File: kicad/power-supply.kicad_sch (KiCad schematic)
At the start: 6 parts, among them U8 M3406

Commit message: added title to all circuit diagrams and sub-circuit diagrams, and PDF export
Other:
- title: (none) -> step-down voltage regulator
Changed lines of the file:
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@@
 (kicad_sch (version 20211123) (generator eeschema)
   (paper "A4")
+  (title_block
+    (title "step-down voltage regulator")
+  )
   (junction (at 133.35 72.39) (diameter 0) (color 0 0 0 0)
   )

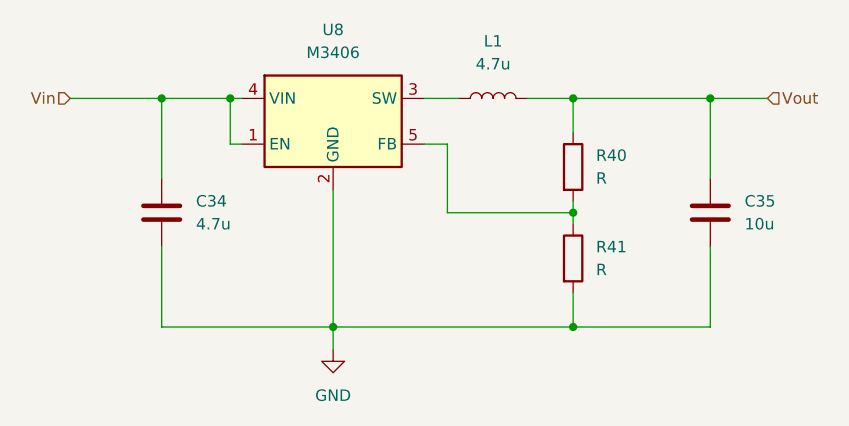
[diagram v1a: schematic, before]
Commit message: new flash, and IEC interface added
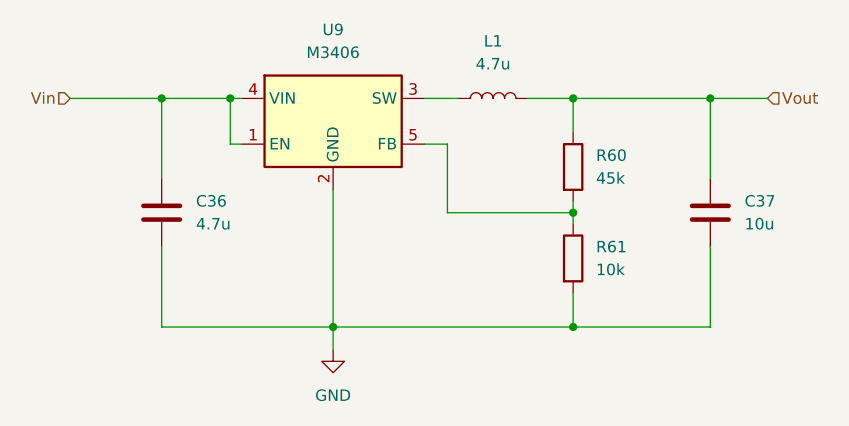
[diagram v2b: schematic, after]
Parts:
- R60: renamed from R40; value R -> 45k; footprint Resistor_SMD:R_0402_1005Metric -> Resistor_SMD:R_0805_2012Metric
- R61: renamed from R41; value R -> 10k; footprint Resistor_SMD:R_0402_1005Metric -> Resistor_SMD:R_0805_2012Metric
- renumbered C34 to C36, C35 to C37, U8 to U9
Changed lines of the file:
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@@
   (symbol (lib_id "Device:R") (at 133.35 67.31 0) (unit 1)
     (in_bom yes) (on_board yes) (fields_autoplaced)
-    (property "Reference" "R40" (id 0) (at 135.89 66.0399 0)
+    (property "Reference" "R60" (id 0) (at 135.89 66.0399 0)
       (effects (font (size 1.27 1.27)) (justify left))
     )
-    (property "Value" "R" (id 1) (at 135.89 68.5799 0)
+    (property "Value" "45k" (id 1) (at 135.89 68.5799 0)
       (effects (font (size 1.27 1.27)) (justify left))
     )
-    (property "Footprint" "Resistor_SMD:R_0402_1005Metric" (id 2) (at 131.572 67.31 90)
+    (property "Footprint" "Resistor_SMD:R_0805_2012Metric" (id 2) (at 131.572 67.31 90)
       (effects (font (size 1.27 1.27)) hide)
     )
@@
   (symbol (lib_id "Device:C") (at 87.63 72.39 0) (unit 1)
     (in_bom yes) (on_board yes) (fields_autoplaced)
-    (property "Reference" "C34" (id 0) (at 91.44 71.1199 0)
+    (property "Reference" "C36" (id 0) (at 91.44 71.1199 0)
       (effects (font (size 1.27 1.27)) (justify left))
     )
@@
   (symbol (lib_id "power:GND") (at 106.68 87.63 0) (unit 1)
     (in_bom yes) (on_board yes) (fields_autoplaced)
-    (property "Reference" "#PWR076" (id 0) (at 106.68 93.98 0)
+    (property "Reference" "#PWR082" (id 0) (at 106.68 93.98 0)
       (effects (font (size 1.27 1.27)) hide)
     )
@@
   (symbol (lib_id "Device:C") (at 148.59 72.39 0) (unit 1)
     (in_bom yes) (on_board yes) (fields_autoplaced)
-    (property "Reference" "C35" (id 0) (at 152.4 71.1199 0)
+    (property "Reference" "C37" (id 0) (at 152.4 71.1199 0)
       (effects (font (size 1.27 1.27)) (justify left))
     )
@@
   (symbol (lib_id "Regulator_Switching:PAM2301CAABADJ") (at 106.68 62.23 0) (unit 1)
     (in_bom yes) (on_board yes) (fields_autoplaced)
-    (property "Reference" "U8" (id 0) (at 106.68 52.07 0))
+    (property "Reference" "U9" (id 0) (at 106.68 52.07 0))
     (property "Value" "M3406" (id 1) (at 106.68 54.61 0))
     (property "Footprint" "Package_TO_SOT_SMD:TSOT-23-5" (id 2) (at 107.95 68.58 0)
@@
   (symbol (lib_id "Device:R") (at 133.35 77.47 0) (unit 1)
     (in_bom yes) (on_board yes) (fields_autoplaced)
-    (property "Reference" "R41" (id 0) (at 135.89 76.1999 0)
+    (property "Reference" "R61" (id 0) (at 135.89 76.1999 0)
       (effects (font (size 1.27 1.27)) (justify left))
     )
-    (property "Value" "R" (id 1) (at 135.89 78.7399 0)
+    (property "Value" "10k" (id 1) (at 135.89 78.7399 0)
       (effects (font (size 1.27 1.27)) (justify left))
     )
-    (property "Footprint" "Resistor_SMD:R_0402_1005Metric" (id 2) (at 131.572 77.47 90)
+    (property "Footprint" "Resistor_SMD:R_0805_2012Metric" (id 2) (at 131.572 77.47 90)
       (effects (font (size 1.27 1.27)) hide)
     )

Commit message: circuit improvements fixed the level shifter circuit, added the shield pins to the reset button, and replaced the IEC circuit with unused pins of the 16 bit level shifter, and a new 6 channel open collector driver
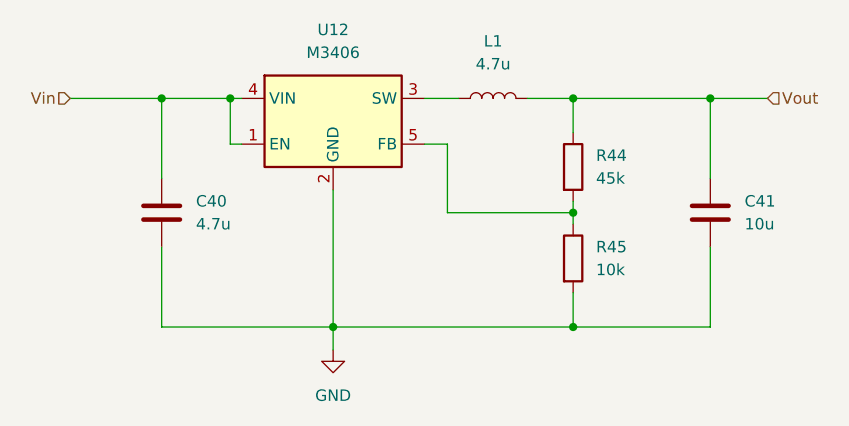
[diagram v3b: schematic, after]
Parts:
- renumbered C36 to C40, C37 to C41, R60 to R44, R61 to R45, U9 to U12
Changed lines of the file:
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@@
   (symbol (lib_id "Device:R") (at 133.35 67.31 0) (unit 1)
     (in_bom yes) (on_board yes) (fields_autoplaced)
-    (property "Reference" "R60" (id 0) (at 135.89 66.0399 0)
+    (property "Reference" "R44" (id 0) (at 135.89 66.0399 0)
       (effects (font (size 1.27 1.27)) (justify left))
     )
@@
   (symbol (lib_id "Device:C") (at 87.63 72.39 0) (unit 1)
     (in_bom yes) (on_board yes) (fields_autoplaced)
-    (property "Reference" "C36" (id 0) (at 91.44 71.1199 0)
+    (property "Reference" "C40" (id 0) (at 91.44 71.1199 0)
       (effects (font (size 1.27 1.27)) (justify left))
     )
@@
   (symbol (lib_id "power:GND") (at 106.68 87.63 0) (unit 1)
     (in_bom yes) (on_board yes) (fields_autoplaced)
-    (property "Reference" "#PWR082" (id 0) (at 106.68 93.98 0)
+    (property "Reference" "#PWR0101" (id 0) (at 106.68 93.98 0)
       (effects (font (size 1.27 1.27)) hide)
     )
@@
   (symbol (lib_id "Device:C") (at 148.59 72.39 0) (unit 1)
     (in_bom yes) (on_board yes) (fields_autoplaced)
-    (property "Reference" "C37" (id 0) (at 152.4 71.1199 0)
+    (property "Reference" "C41" (id 0) (at 152.4 71.1199 0)
       (effects (font (size 1.27 1.27)) (justify left))
     )
@@
   (symbol (lib_id "Regulator_Switching:PAM2301CAABADJ") (at 106.68 62.23 0) (unit 1)
     (in_bom yes) (on_board yes) (fields_autoplaced)
-    (property "Reference" "U9" (id 0) (at 106.68 52.07 0))
+    (property "Reference" "U12" (id 0) (at 106.68 52.07 0))
     (property "Value" "M3406" (id 1) (at 106.68 54.61 0))
     (property "Footprint" "Package_TO_SOT_SMD:TSOT-23-5" (id 2) (at 107.95 68.58 0)
@@
   (symbol (lib_id "Device:R") (at 133.35 77.47 0) (unit 1)
     (in_bom yes) (on_board yes) (fields_autoplaced)
-    (property "Reference" "R61" (id 0) (at 135.89 76.1999 0)
+    (property "Reference" "R45" (id 0) (at 135.89 76.1999 0)
       (effects (font (size 1.27 1.27)) (justify left))
     )

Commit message: started routing
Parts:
- renumbered R44 to R48, R45 to R49
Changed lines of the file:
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@@
   (symbol (lib_id "Device:R") (at 133.35 67.31 0) (unit 1)
     (in_bom yes) (on_board yes) (fields_autoplaced)
-    (property "Reference" "R44" (id 0) (at 135.89 66.0399 0)
+    (property "Reference" "R48" (id 0) (at 135.89 66.0399 0)
       (effects (font (size 1.27 1.27)) (justify left))
     )
@@
   (symbol (lib_id "power:GND") (at 106.68 87.63 0) (unit 1)
     (in_bom yes) (on_board yes) (fields_autoplaced)
-    (property "Reference" "#PWR0101" (id 0) (at 106.68 93.98 0)
+    (property "Reference" "#PWR0105" (id 0) (at 106.68 93.98 0)
       (effects (font (size 1.27 1.27)) hide)
     )
@@
   (symbol (lib_id "Device:R") (at 133.35 77.47 0) (unit 1)
     (in_bom yes) (on_board yes) (fields_autoplaced)
-    (property "Reference" "R45" (id 0) (at 135.89 76.1999 0)
+    (property "Reference" "R49" (id 0) (at 135.89 76.1999 0)
       (effects (font (size 1.27 1.27)) (justify left))
     )

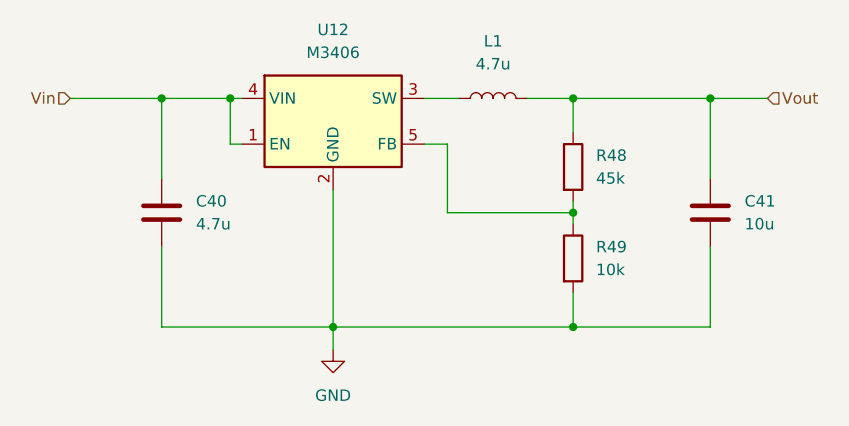
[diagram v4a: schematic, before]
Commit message: board fully routed
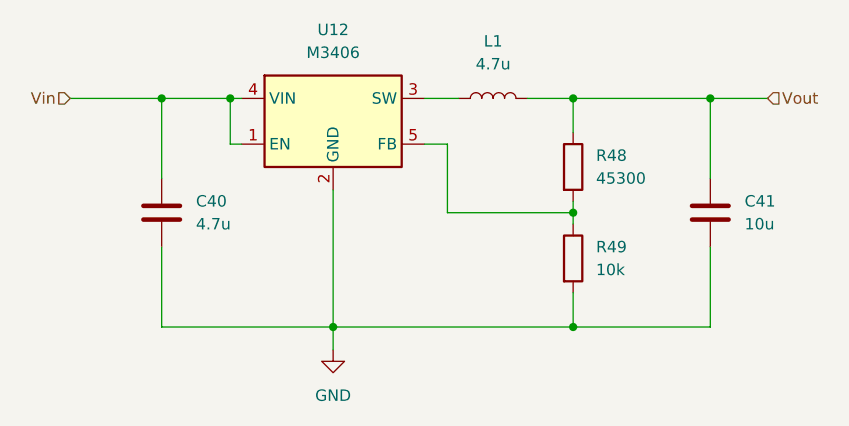
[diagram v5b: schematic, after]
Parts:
- R48: value 45k -> 45300
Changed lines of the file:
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@@
       (effects (font (size 1.27 1.27)) (justify left))
     )
-    (property "Value" "45k" (id 1) (at 135.89 68.5799 0)
+    (property "Value" "45300" (id 1) (at 135.89 68.5799 0)
       (effects (font (size 1.27 1.27)) (justify left))
     )

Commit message: first successful Gowin FPGA configuration from RP2040
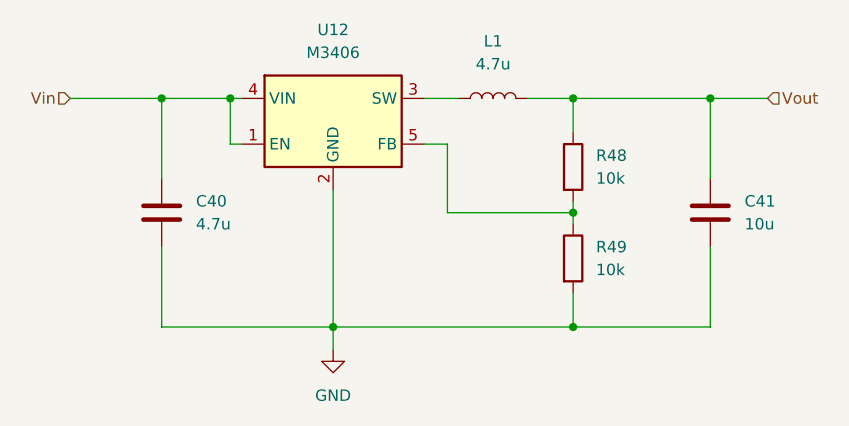
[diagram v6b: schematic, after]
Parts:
- R48: value 45300 -> 10k
